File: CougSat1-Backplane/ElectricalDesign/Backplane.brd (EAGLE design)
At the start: 82.8 x 86 mm, 20 parts, among them J1 CougSat Socket, J10 CougSat Socket, J2 CougSat Socket, J3 CougSat Socket, J4 CougSat Socket, J5 Separation Switch, J6 Separation Switch, J7 CougSat Socket, J8 CougSat Socket, J9 CougSat Socket

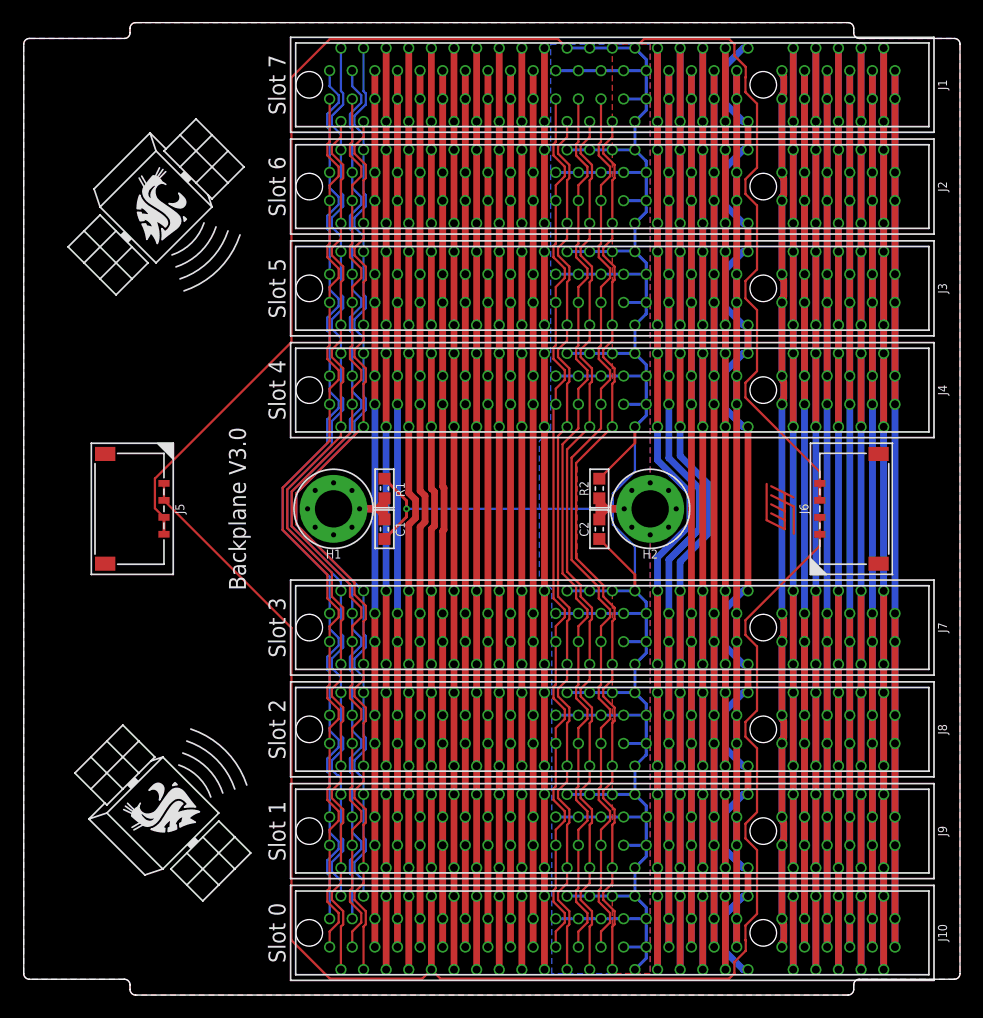
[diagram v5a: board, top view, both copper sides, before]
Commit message: Switched CTRL_RESET to GPIO pins
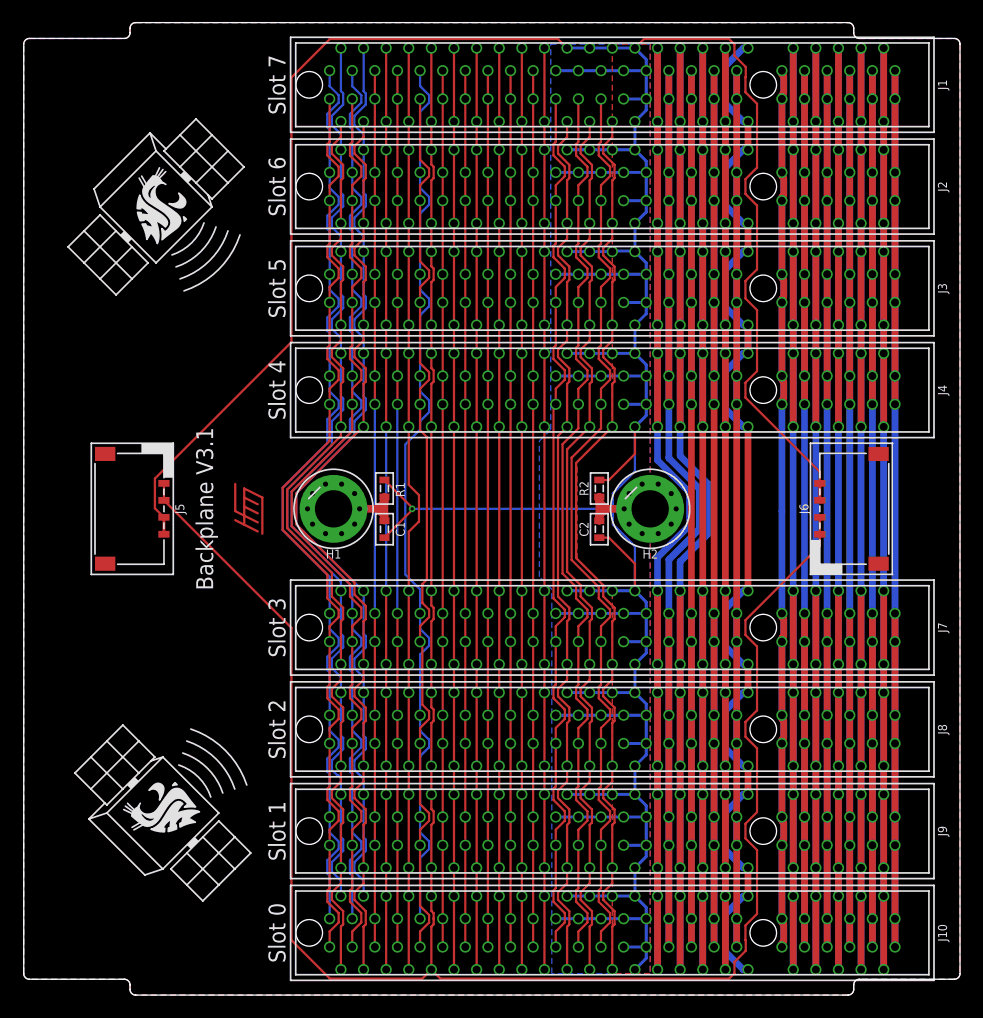
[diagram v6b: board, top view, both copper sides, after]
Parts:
- moved LOGO2 47.0 mm to (-21.5, 0.00), turned to 90 degrees
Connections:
- removed net CTRL_!RESET: J1.A41, J1.B41, J10.A41, J10.B41, J2.A41, J2.B41, J3.A41, J3.B41, J4.A41, J4.B41, J7.A41, J7.B41, J8.A41, J8.B41, J9.A41, J9.B41
- new net GPIO-6: J1.A41, J10.A41, J2.A41, J3.A41, J4.A41, J7.A41, J8.A41, J9.A41
- new net GPIO-7: J1.B41, J10.B41, J2.B41, J3.B41, J4.B41, J7.B41, J8.B41, J9.B41
- net CHASSIS1: now also H1.V10, H1.V9
- net CHASSIS2: now also H2.V10, H2.V9
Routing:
- net GPIO-7: track 0.00 -> 80.7 mm
- net GPIO-6: track 0.00 -> 80.0 mm
- net CTRL_!RESET: track 77.9 -> 0.00 mm
- net PR_BATT-6: track 144.4 -> 150.9 mm
- net PR_BATT-4: track 144.1 -> 150.6 mm
- net PR_BATT-5: track 136.2 -> 138.7 mm
- net CHASSIS2: track 26.5 -> 28.8 mm
- net CHASSIS1: track 26.2 -> 28.4 mm
- net PWR_CTRL_SW: track 214.3 -> 215.2 mm
- net PGND: track 382.0 -> 382.9 mm
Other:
- board text added: "Backplane V3.1"
- board text removed: "Backplane V3.0"

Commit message: Removed Unused Connectors, Shrunk Outline
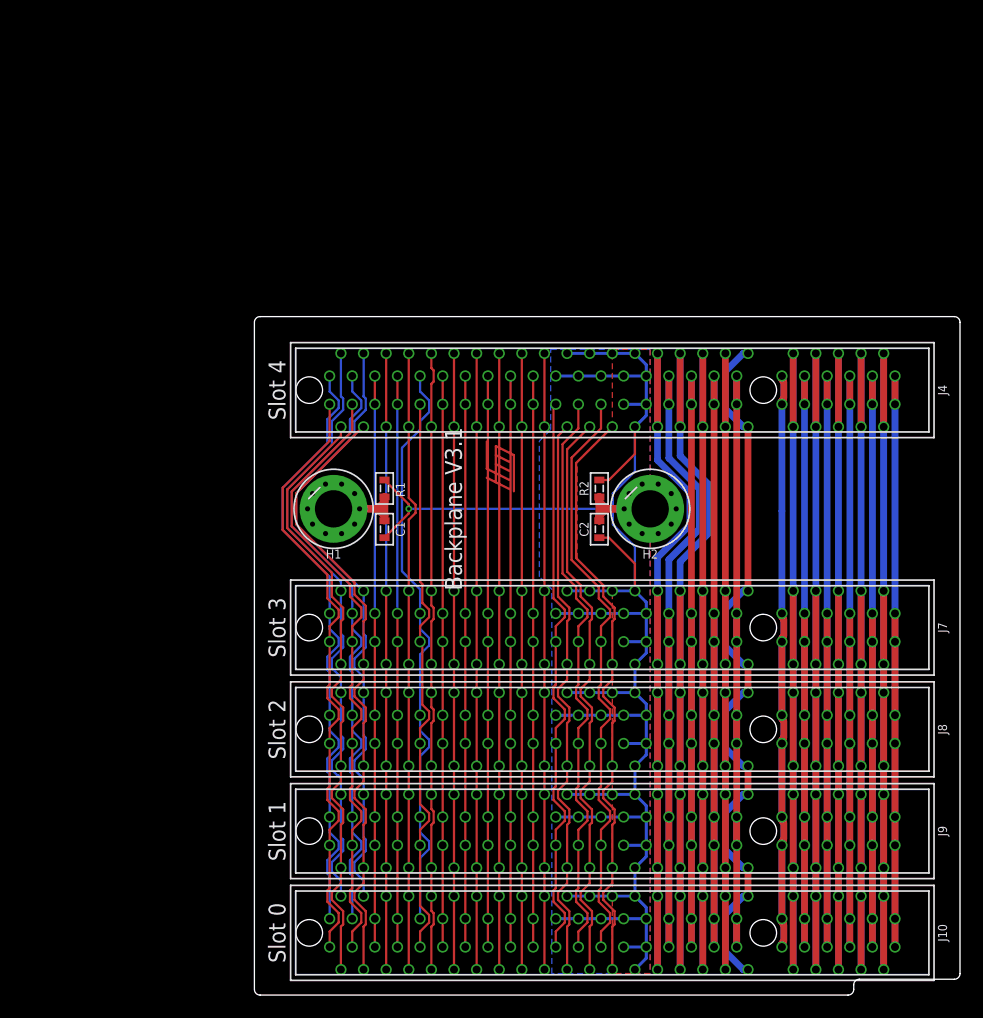
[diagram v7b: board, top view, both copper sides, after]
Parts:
- removed J1, J2, J3: CougSat Socket, CougsInSpace-Connectors:PCIE-8
- removed J5, J6: Separation Switch, CougsInSpace-Connectors:PICOLOCK1.5-04
- removed LOGO1: Text, CougsInSpace-Aesthetics:CIS-TEXT
- removed LOGO100, LOGO3: Satellite 16mm, CougsInSpace-Aesthetics:CIS-SATELLITE-16
- moved LOGO2 22.6 mm to (0.75, 3.75)
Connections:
- net BUS_I2C0_IRQ: no longer J1.A45, J1.B45, J2.A45, J2.B45, J3.A45, J3.B45
- net BUS_I2C0_SCL: no longer J1.A44, J1.B44, J2.A44, J2.B44, J3.A44, J3.B44
- net BUS_I2C0_SDA: no longer J1.A43, J1.B43, J2.A43, J2.B43, J3.A43, J3.B43
- net BUS_I2C1_IRQ: no longer J1.A32, J1.B32, J2.A32, J2.B32, J3.A32, J3.B32
- net BUS_I2C1_SCL: no longer J1.A31, J1.B31, J2.A31, J2.B31, J3.A31, J3.B31
- net BUS_I2C1_SDA: no longer J1.A30, J1.B30, J2.A30, J2.B30, J3.A30, J3.B30
- net BUS_JTAG_EN-0: no longer J1.B46, J2.B46, J3.B46
- net BUS_JTAG_EN-1: no longer J1.B47, J2.B47, J3.B47
- net BUS_JTAG_EN-2: no longer J1.B48, J2.B48, J3.B48
- net BUS_JTAG_EN-3: no longer J1.B49, J2.B49, J3.B49
- net BUS_JTAG_TCK: no longer J1.A46, J2.A46, J3.A46
- net BUS_JTAG_TDI: no longer J1.A47, J2.A47, J3.A47
- net BUS_JTAG_TDO: no longer J1.A48, J2.A48, J3.A48
- net BUS_JTAG_TMS: no longer J1.A49, J2.A49, J3.A49
- net BUS_SPI_MISO: no longer J1.A38, J1.B38, J2.A38, J2.B38, J3.A38, J3.B38
- net BUS_SPI_MOSI: no longer J1.A39, J1.B39, J2.A39, J2.B39, J3.A39, J3.B39
- net BUS_SPI_SCK: no longer J1.A37, J1.B37, J2.A37, J2.B37, J3.A37, J3.B37
- net COM_SPI_CS: no longer J1.A36, J1.B36, J2.A36, J2.B36, J3.A36, J3.B36
- net COM_SPI_MISO: no longer J1.A34, J1.B34, J2.A34, J2.B34, J3.A34, J3.B34
- net COM_SPI_MOSI: no longer J1.A35, J1.B35, J2.A35, J2.B35, J3.A35, J3.B35
- net COM_SPI_SCK: no longer J1.A33, J1.B33, J2.A33, J2.B33, J3.A33, J3.B33
- net CTRL_SYNC: no longer J1.A42, J1.B42, J2.A42, J2.B42, J3.A42, J3.B42
- net GPIO-0: no longer J1.A24, J2.A24, J3.A24
- net GPIO-1: no longer J1.A25, J2.A25, J3.A25
- net GPIO-2: no longer J1.A26, J2.A26, J3.A26
- net GPIO-3: no longer J1.A27, J2.A27, J3.A27
- net GPIO-4: no longer J1.A28, J2.A28, J3.A28
- net GPIO-5: no longer J1.A29, J2.A29, J3.A29
- net GPIO-6: no longer J1.A41, J2.A41, J3.A41
- net GPIO-7: no longer J1.B41, J2.B41, J3.B41
- net PGND: no longer J1.A21, J1.A22, J1.A23, J1.B21, J1.B22, J1.B23, J1.B24, J1.B25, J1.B26, J1.B27, J1.B28, J1.B29, J2.A21, J2.A22, J2.A23, J2.B21, J2.B22, J2.B23, J2.B24, J2.B25, J2.B26, J2.B27, J2.B28, J2.B29, J3.A21, J3.A22, J3.A23, J3.B21, J3.B22, J3.B23, J3.B24, J3.B25, J3.B26, J3.B27, J3.B28, J3.B29, J5.3, J5.4, J6.3, J6.4
- net PR_3.3V-0: no longer J1.A1, J1.B1, J2.A1, J2.B1, J3.A1, J3.B1
- net PR_3.3V-1: no longer J1.A2, J1.B2, J2.A2, J2.B2, J3.A2, J3.B2
- net PR_3.3V-10: no longer J1.A11, J1.B11, J2.A11, J2.B11, J3.A11, J3.B11
- net PR_3.3V-11: no longer J1.A12, J1.B12, J2.A12, J2.B12, J3.A12, J3.B12
- net PR_3.3V-12: no longer J1.A13, J1.B13, J2.A13, J2.B13, J3.A13, J3.B13
- net PR_3.3V-2: no longer J1.A3, J1.B3, J2.A3, J2.B3, J3.A3, J3.B3
- net PR_3.3V-3: no longer J1.A4, J1.B4, J2.A4, J2.B4, J3.A4, J3.B4
- net PR_3.3V-4: no longer J1.A5, J1.B5, J2.A5, J2.B5, J3.A5, J3.B5
- net PR_3.3V-5: no longer J1.A6, J1.B6, J2.A6, J2.B6, J3.A6, J3.B6
- net PR_3.3V-6: no longer J1.A7, J1.B7, J2.A7, J2.B7, J3.A7, J3.B7
- net PR_3.3V-7: no longer J1.A8, J1.B8, J2.A8, J2.B8, J3.A8, J3.B8
- net PR_3.3V-8: no longer J1.A9, J1.B9, J2.A9, J2.B9, J3.A9, J3.B9
- net PR_3.3V-9: no longer J1.A10, J1.B10, J2.A10, J2.B10, J3.A10, J3.B10
- net PR_BATT-0: no longer J1.A14, J1.B14, J2.A14, J2.B14, J3.A14, J3.B14
- net PR_BATT-1: no longer J1.A15, J1.B15, J2.A15, J2.B15, J3.A15, J3.B15
- net PR_BATT-2: no longer J1.A16, J1.B16, J2.A16, J2.B16, J3.A16, J3.B16
- net PR_BATT-3: no longer J1.A17, J1.B17, J2.A17, J2.B17, J3.A17, J3.B17
- net PR_BATT-4: no longer J1.A18, J1.B18, J2.A18, J2.B18, J3.A18, J3.B18
- net PR_BATT-5: no longer J1.A19, J1.B19, J2.A19, J2.B19, J3.A19, J3.B19
- net PR_BATT-6: no longer J1.A20, J1.B20, J2.A20, J2.B20, J3.A20, J3.B20
- net PWR_CTRL_SW: no longer J1.A40, J1.B40, J2.A40, J2.B40, J3.A40, J3.B40, J5.1, J5.2, J6.1, J6.2
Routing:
- net PGND: track 382.9 -> 178.2 mm
- net PWR_CTRL_SW: track 215.2 -> 55.3 mm
- net PR_3.3V-10: track 138.6 -> 83.8 mm
- net PR_BATT-4: track 150.6 -> 96.6 mm
- net PR_BATT-3: track 136.5 -> 82.5 mm
- net PR_BATT-2: track 148.5 -> 94.5 mm
- net PR_BATT-1: track 136.5 -> 82.5 mm
- net PR_3.3V-9: track 148.5 -> 94.5 mm
- net PR_3.3V-8: track 136.5 -> 82.5 mm
- net PR_3.3V-7: track 148.5 -> 94.5 mm
- net PR_3.3V-6: track 136.5 -> 82.5 mm
- net PR_3.3V-5: track 148.5 -> 94.5 mm
- net PR_3.3V-4: track 136.5 -> 82.5 mm
- net PR_3.3V-3: track 148.5 -> 94.5 mm
- net PR_3.3V-2: track 136.5 -> 82.5 mm
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- removed copper zone on layer 1, net BALANCING-TOP
- removed copper zone on layer 16, net BALANCING-TOP
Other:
- board size 82.8 x 86 mm -> 62.4 x 60 mm
- board text removed: "Slot 5"
- board text removed: "Slot 6"
- board text removed: "Slot 7"

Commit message: Made board and schematic pretty again
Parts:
- moved LOGO2 22.1 mm to (22.5, 0.00), flipped to the bottom
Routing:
- net PR_3.3V-8: track 82.5 -> 101.0 mm
- net PR_3.3V-6: track 82.5 -> 101.0 mm
- net PR_3.3V-4: track 82.5 -> 101.0 mm
- net PR_3.3V-2: track 82.5 -> 101.0 mm
- net PR_3.3V-10: track 83.8 -> 102.3 mm
- net PR_3.3V-0: track 82.5 -> 101.0 mm
- net PR_3.3V-9: track 94.5 -> 109.0 mm
- net PR_3.3V-7: track 94.5 -> 109.0 mm
- net PR_3.3V-5: track 94.5 -> 109.0 mm
- net PR_3.3V-3: track 94.5 -> 109.0 mm
- net PR_3.3V-1: track 94.5 -> 109.0 mm
- net PR_3.3V-11: track 65.2 -> 72.7 mm
- added copper zone on layer 16, net BALANCING-BOTTOM
- added copper zone on layer 1, net BALANCING-BOTTOM1
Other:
- board text added: "Backplane V3.2"
- board text removed: "Backplane V3.1"
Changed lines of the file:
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@@
 <wire x1="-21" y1="-42.5" x2="-21" y2="16.5" width="0" layer="20"/>
 <wire x1="-21" y1="16.5" x2="-20.5" y2="17" width="0" layer="20" curve="-90"/>
-<text x="-3.4" y="0" size="1.5" layer="21" font="vector" ratio="15" rot="R90" align="center">Backplane V3.1</text>
+<text x="30" y="0.1" size="1.5" layer="21" font="vector" ratio="15" rot="R180" align="center">Backplane V3.2</text>
 <text x="-19" y="-37.5" size="1.5" layer="21" font="vector" ratio="15" rot="R270" align="center">Slot 0</text>
 <text x="-19" y="-28.5" size="1.5" layer="21" font="vector" ratio="15" rot="R270" align="center">Slot 1</text>
@@
 <attribute name="TEMP" value="70°C Max 2A" x="-85.75" y="-37.57" size="1.778" layer="27" rot="R270" display="off"/>
 </element>
-<element name="LOGO2" library="CougsInSpace-Aesthetics" package="SIGN-HENDRIK" value="SIGNATUREHENDRIK" x="0.75" y="3.75" smashed="yes" rot="R90"/>
+<element name="LOGO2" library="CougsInSpace-Aesthetics" package="SIGN-HENDRIK" value="SIGNATUREHENDRIK" x="22.5" y="0" smashed="yes" rot="MR90"/>
 </elements>
 <signals>
@@
 <wire x1="35.65" y1="11.75" x2="35.65" y2="9.25" width="0.6" layer="16"/>
 <wire x1="35.65" y1="9.25" x2="35.65" y2="-9.25" width="0.6" layer="16"/>
+<wire x1="35.65" y1="9.25" x2="35.65" y2="-9.25" width="0.6" layer="1"/>
 </signal>
 <signal name="PR_3.3V-1">
@@
 <wire x1="34.65" y1="7.25" x2="34.65" y2="13.75" width="0.6" layer="16"/>
 <wire x1="34.65" y1="-7.25" x2="34.65" y2="7.25" width="0.6" layer="16"/>
+<wire x1="34.65" y1="-7.25" x2="34.65" y2="7.25" width="0.6" layer="1"/>
 </signal>
 <signal name="PR_3.3V-2">
@@
 <wire x1="33.65" y1="11.75" x2="33.65" y2="9.25" width="0.6" layer="16"/>
 <wire x1="33.65" y1="9.25" x2="33.65" y2="-9.25" width="0.6" layer="16"/>
+<wire x1="33.65" y1="9.25" x2="33.65" y2="-9.25" width="0.6" layer="1"/>
 </signal>
 <signal name="PR_3.3V-3">
@@
 <wire x1="32.65" y1="7.25" x2="32.65" y2="13.75" width="0.6" layer="16"/>
 <wire x1="32.65" y1="-7.25" x2="32.65" y2="7.25" width="0.6" layer="16"/>
+<wire x1="32.65" y1="-7.25" x2="32.65" y2="7.25" width="0.6" layer="1"/>
 </signal>
 <signal name="PR_3.3V-4">
@@
 <wire x1="31.65" y1="11.75" x2="31.65" y2="9.25" width="0.6" layer="16"/>
 <wire x1="31.65" y1="9.25" x2="31.65" y2="-9.25" width="0.6" layer="16"/>
+<wire x1="31.65" y1="9.25" x2="31.65" y2="-9.25" width="0.6" layer="1"/>
 </signal>
 <signal name="PR_3.3V-5">
@@
 <wire x1="30.65" y1="7.25" x2="30.65" y2="13.75" width="0.6" layer="16"/>
 <wire x1="30.65" y1="-7.25" x2="30.65" y2="7.25" width="0.6" layer="16"/>
+<wire x1="30.65" y1="-7.25" x2="30.65" y2="7.25" width="0.6" layer="1"/>
 </signal>
 <signal name="PR_3.3V-6">
@@
 <wire x1="29.65" y1="11.75" x2="29.65" y2="9.25" width="0.6" layer="16"/>
 <wire x1="29.65" y1="-9.25" x2="29.65" y2="9.25" width="0.6" layer="16"/>
+<wire x1="29.65" y1="9.25" x2="29.65" y2="-9.25" width="0.6" layer="1"/>
 </signal>
 <signal name="PR_3.3V-7">
@@
 <wire x1="28.65" y1="7.25" x2="28.65" y2="13.75" width="0.6" layer="16"/>
 <wire x1="28.65" y1="7.25" x2="28.65" y2="-7.25" width="0.6" layer="16"/>
+<wire x1="28.65" y1="-7.25" x2="28.65" y2="7.25" width="0.6" layer="1"/>
 </signal>
 <signal name="PR_3.3V-8">
@@
 <wire x1="27.65" y1="11.75" x2="27.65" y2="9.25" width="0.6" layer="16"/>
 <wire x1="27.65" y1="-9.25" x2="27.65" y2="9.25" width="0.6" layer="16"/>
+<wire x1="27.65" y1="9.25" x2="27.65" y2="-9.25" width="0.6" layer="1"/>
 </signal>
 <signal name="PR_3.3V-9">
@@
 <wire x1="26.65" y1="7.25" x2="26.65" y2="13.75" width="0.6" layer="16"/>
 <wire x1="26.65" y1="7.25" x2="26.65" y2="-7.25" width="0.6" layer="16"/>
+<wire x1="26.65" y1="-7.25" x2="26.65" y2="7.25" width="0.6" layer="1"/>
 </signal>
 <signal name="PR_3.3V-10">
@@
 <wire x1="25.81" y1="11.24973125" x2="25.65" y2="11.40973125" width="0.6" layer="16"/>
 <wire x1="25.65" y1="11.40973125" x2="25.65" y2="11.75" width="0.6" layer="16"/>
-<wire x1="25.65" y1="-9.25" x2="25.65" y2="-0.2" width="0.6" layer="16"/>
-<wire x1="25.65" y1="-0.2" x2="25.65" y2="9.25" width="0.6" layer="16"/>
+<wire x1="25.65" y1="9.25" x2="25.65" y2="-9.25" width="0.6" layer="1"/>
+<wire x1="25.65" y1="9.25" x2="25.65" y2="-9.25" width="0.6" layer="16"/>
 </signal>
 <signal name="PR_3.3V-11">
@@
 <wire x1="22.23578125" y1="13.75" x2="22.65" y2="13.75" width="0.6" layer="16"/>
 <wire x1="20.65" y1="12.16421875" x2="22.23578125" y2="13.75" width="0.6" layer="16"/>
+<wire x1="22.65" y1="-22.75" x2="22.65" y2="-25.25" width="0.6" layer="16"/>
+<wire x1="22.65" y1="-34.25" x2="22.65" y2="-31.75" width="0.6" layer="16"/>
+<wire x1="22.65" y1="-13.75" x2="22.65" y2="-16.25" width="0.6" layer="16"/>
 </signal>
 <signal name="PR_3.3V-12">
@@
 <wire x1="-7.95" y1="-5.518625" x2="-7.95" y2="5.4" width="0.2" layer="16"/>
 </signal>
+<signal name="BALANCING-BOTTOM">
+<polygon width="0.16" layer="16" spacing="0.5" pour="hatch">
+<vertex x="-21" y="-42.5"/>
+<vertex x="-21" y="16.5" curve="-90"/>
+<vertex x="-20.5" y="17"/>
+<vertex x="40.9" y="17" curve="-90"/>
+<vertex x="41.4" y="16.5"/>
+<vertex x="41.4" y="-41.6"/>
+<vertex x="32.5" y="-41.6" curve="90"/>
+<vertex x="32" y="-42.1"/>
+<vertex x="32" y="-42.5" curve="-90"/>
+<vertex x="31.5" y="-43"/>
+<vertex x="-20.5" y="-43" curve="-90"/>
+</polygon>
+</signal>
+<signal name="BALANCING-BOTTOM1">
+<polygon width="0.16" layer="1" spacing="0.5" pour="hatch">
+<vertex x="-21" y="-42.5"/>
+<vertex x="-21" y="16.5" curve="-90"/>
+<vertex x="-20.5" y="17"/>
+<vertex x="40.9" y="17" curve="-90"/>
+<vertex x="41.4" y="16.5"/>
+<vertex x="41.4" y="-41.6"/>
+<vertex x="32.5" y="-41.6" curve="90"/>
+<vertex x="32" y="-42.1"/>
+<vertex x="32" y="-42.5" curve="-90"/>
+<vertex x="31.5" y="-43"/>
+<vertex x="-20.5" y="-43" curve="-90"/>
+</polygon>
+</signal>
 </signals>
